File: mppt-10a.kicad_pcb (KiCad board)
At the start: 2 copper layers, 80 x 80 mm, 133 parts, among them J1 SOLAR, J2 LOAD, J3 BAT, J4 UEXT, J5 USB_A_stacked, P1 CONN_01X02, Q1 PSMN5R2-60YLX, Q2 PSMN5R2-60YLX, Q3 PSMN5R2-60YLX, Q4 PSMN5R2-60YLX, SW2 SW_PUSH, T1 MMBT3904, T3 MMBT3904, U1 LM5109BMA, U2 STM32F072CB, U3 AP22802A, U4 IP4220CZ6, U5 AP2210-3.3, U6 24AA01, U7 LM258, U8 TPS2513, U9 AP6502, Y1 8MHz

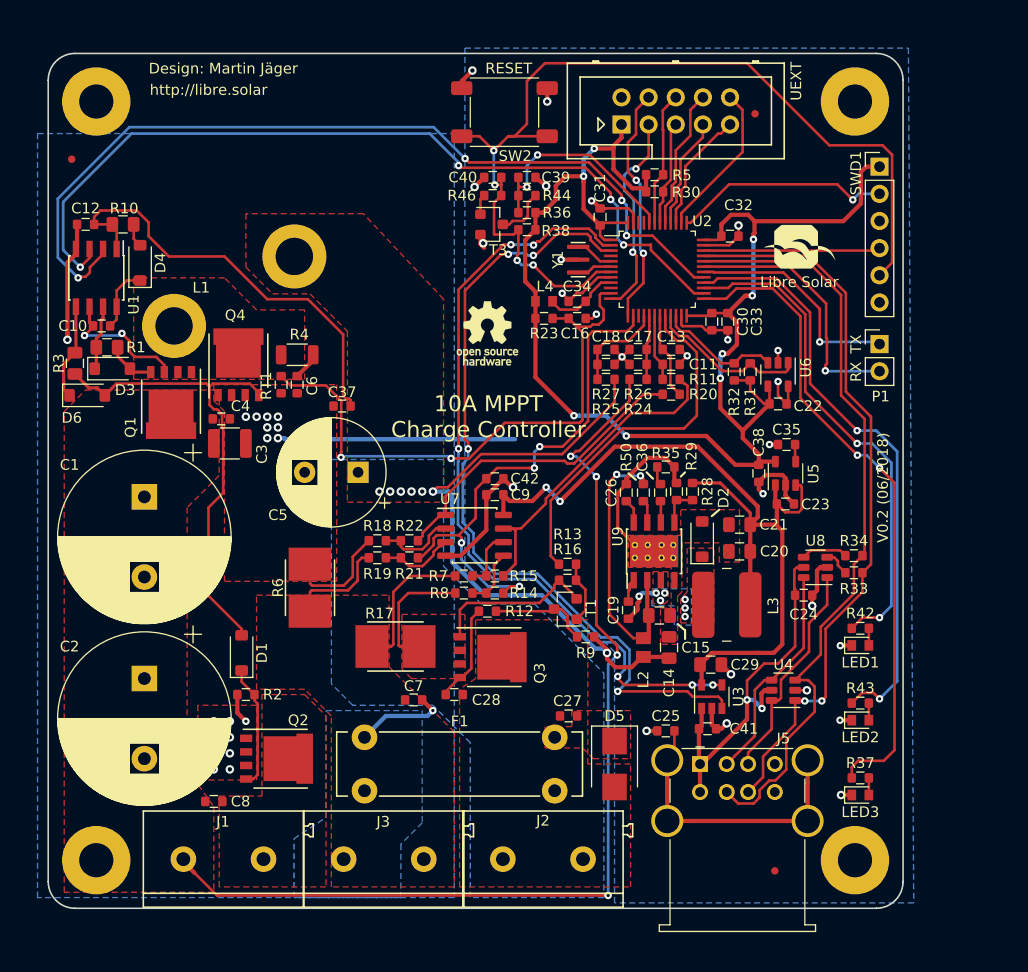
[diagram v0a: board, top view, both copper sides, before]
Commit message: Several improvements (v0.4) after first tests
- Ultra-low-power MCU STM32L072
- Larger screw terminals
- USB power supply replaced by more efficient SMPS
- High-side load switch with P-MOS
- High-side current measurement to include USB current in load measurement
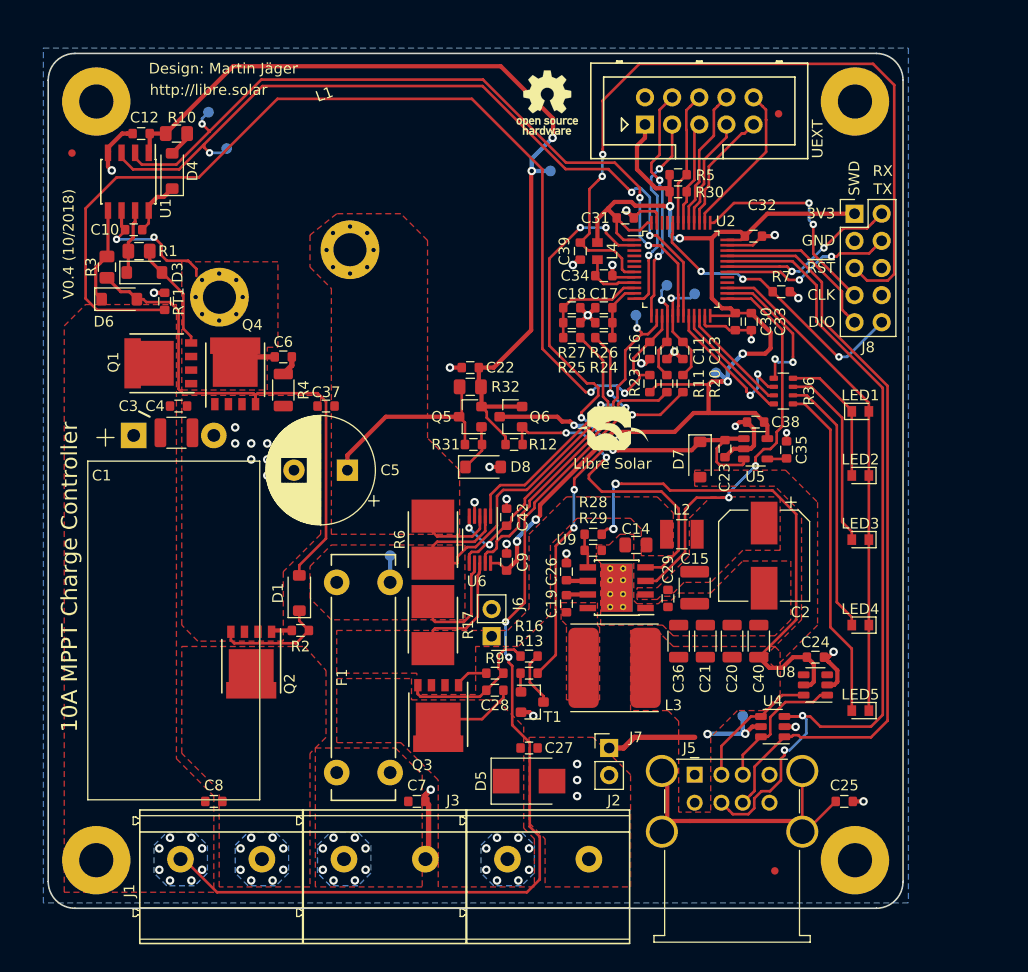
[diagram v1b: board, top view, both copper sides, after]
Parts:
- removed C41: 100n, LibreSolar:C_0603_1608
- removed D2: SS14FL, LibreSolar:D_SOD-123
- removed P1: CONN_01X02, Connector_PinHeader_2.54mm:PinHeader_1x02_P2.54mm_Vertical
- removed R14, R15, R21, R22: 150k, LibreSolar:R_0603_1608
- removed R18, R19, R44, R8: 2.2k, LibreSolar:R_0603_1608
- removed R33, R34: 0R, LibreSolar:R_0603_1608
- removed R35: 6.8k, LibreSolar:R_0603_1608
- removed R37, R42, R43: 470, LibreSolar:R_0603_1608
- removed R38: 1M, LibreSolar:R_0603_1608
- removed R46: 56k, LibreSolar:R_0603_1608
- removed R50: 100k, LibreSolar:R_0603_1608
- removed SW2: SW_PUSH, LibreSolar:SW_SPST_6mm
- removed SWD1: ST_Nucleo_SWD, Connector_PinHeader_2.54mm:PinHeader_1x06_P2.54mm_Vertical
- removed T3: MMBT3904, LibreSolar:SOT-23
- removed U3: AP22802A, Package_TO_SOT_SMD:SOT-23-5
- removed U7: LM258, LibreSolar:SOIC-8_3.9x4.9mm_Pitch1.27mm
- removed Y1: 8MHz, LibreSolar:Resonator_Murata_CSTCE_G
- added D7: 1N4148, LibreSolar:D_SOD-123, F.Cu at (159.5, 96.0)
- added D8: 11V, LibreSolar:D_SOD-123, F.Cu at (139.2, 96.7)
- added J6: PWR_12V, Connector_PinHeader_2.54mm:PinHeader_1x02_P2.54mm_Vertical, F.Cu at (140.0, 112.5)
- added J7: PWR_5V, Connector_PinHeader_2.54mm:PinHeader_1x02_P2.54mm_Vertical, F.Cu at (151.0, 123.0)
- added J8: Conn_02x05_Odd_Even, Connector_PinHeader_2.54mm:PinHeader_2x05_P2.54mm_Vertical, F.Cu at (174.0, 73.0)
- added LED4: green, LED_SMD:LED_0603_1608Metric, F.Cu at (174.5, 111.5)
- added LED5: green, LED_SMD:LED_0603_1608Metric, F.Cu at (174.5, 119.5)
- added Q5: BSS138N, LibreSolar:SOT-23, F.Cu at (138.0, 92.0)
- added Q6: DMP3099L-7, LibreSolar:SOT-23, F.Cu at (141.8, 92.0)
- added TP1: Test_Point_Probe, TestPoint:TestPoint_Pad_D1.0mm, B.Cu at (130.5, 105.0)
- added TP2: Test_Point_Probe, TestPoint:TestPoint_Pad_D1.0mm, B.Cu at (113.5, 63.5)
- added TP3: Test_Point_Probe, TestPoint:TestPoint_Pad_D1.0mm, B.Cu at (115.2, 66.9)
- added TP4: Test_Point_Probe, TestPoint:TestPoint_Pad_D1.0mm, B.Cu at (159.0, 80.5)
- added TP5: Test_Point_Probe, TestPoint:TestPoint_Pad_D1.0mm, B.Cu at (156.4, 79.7)
- added TP6: Test_Point_Probe, TestPoint:TestPoint_Pad_D1.0mm, B.Cu at (153.5, 82.5)
- added TP7: Test_Point_Probe, TestPoint:TestPoint_Pad_D1.0mm, B.Cu at (163.5, 120.0)
- added TP8: Test_Point_Probe, TestPoint:TestPoint_Pad_D1.0mm, B.Cu at (145.5, 69.0)
- added TP9: Test_Point_Probe, TestPoint:TestPoint_Pad_D1.0mm, B.Cu at (161.0, 87.9)
- C1: value 680u -> 1200u; footprint Capacitor_THT:CP_Radial_D16.0mm_P7.50mm -> LibreSolar:CP_Radial_L31.5mm_D16.0mm_P7.50mm_horizontal
- C15: value 22u -> 10u; footprint LibreSolar:C_0805_2012 -> LibreSolar:C_1210_3225
- C2: value 680u -> 150u; footprint Capacitor_THT:CP_Radial_D16.0mm_P7.50mm -> Capacitor_SMD:CP_Elec_8x6.2
- C20, C21: value 47u -> 22u; footprint LibreSolar:C_0805_2012 -> LibreSolar:C_1206_3216
- C22: value 100n -> 2.2u
- C29: value 1u -> 220n; footprint LibreSolar:C_0805_2012 -> LibreSolar:C_0603_1608
- C36: value 6.8n -> 22u; footprint LibreSolar:C_0603_1608 -> LibreSolar:C_1206_3216
- C39: value 2.2u -> 100n
- C40: value 100n -> 22u; footprint LibreSolar:C_0603_1608 -> LibreSolar:C_1206_3216
- J1, J2, J3: footprint LibreSolar:Phoenix_Contact_PT_2,5-2-7,5-H -> LibreSolar:Phoenix_Contact_MKDS_5-2-7,62
- L1: footprint LibreSolar:L-FERYSTER-DTMSS-27 -> LibreSolar:L-FERYSTER-DTMSS-27_33uH
- L2: footprint Inductor_SMD:L_0805_2012Metric -> Inductor_SMD:L_1210_3225Metric
- L3: footprint LibreSolar:Bourns_SRN6045TA -> LibreSolar:Bourns_SRN8040TA
- LED1: value LED_red -> red
- LED2, LED3: value LED_green -> red
- Q3: value PSMN5R2-60YLX -> BSC084P03NS3
- R12: value 2.2k -> 100k
- R27: value 10k -> 5.6k
- R28: value 45.3k -> 100k
- R29: value 10k -> 24.9k
- R31: value 2.2k -> 10k
- R32: value 2.2k -> 4.7; footprint LibreSolar:R_0603_1608 -> LibreSolar:R_0805_2012
- R36: value 1M -> 680; footprint LibreSolar:R_0603_1608 -> LibreSolar:R_Array_Convex_4x0603
- R9: value 56k -> 10k
- U2: value STM32F072CB -> STM32L072CZT6
- U6: value 24AA01 -> INA2181; footprint LibreSolar:SOT-23-5 -> LibreSolar:VSSOP-10_3.0x3.0mm_P0.5mm
- U9: value AP6502 -> LMR33630
- moved C2 59.1 mm to (165.5, 105.0)
- moved C40 50.0 mm to (165.0, 113.0), turned to 90 degrees
- moved R7 39.9 mm to (167.1, 80.3), turned to 0 degrees
- moved U6 31.9 mm to (138.9, 103.5)
- moved R36 29.2 mm to (167.3, 89.6)
- moved C22 29.0 mm to (138.0, 87.4), turned to 180 degrees
- moved R31 26.8 mm to (138.3, 94.6), turned to 180 degrees
- moved R32 24.7 mm to (138.0, 89.2), turned to 0 degrees
- moved LOGO1 24.4 mm to (149.0, 95.1)
- moved LED3 23.9 mm to (174.5, 103.5), turned to 180 degrees
- moved LED2 22.9 mm to (174.5, 97.5), turned to 180 degrees
- moved LOGO2 22.3 mm to (145.2, 62.6)
- moved LED1 21.9 mm to (174.5, 91.5)
- moved C25 18.0 mm to (173.0, 128.0), turned to 0 degrees
- moved R12 15.8 mm to (142.1, 94.6), turned to 180 degrees
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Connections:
- net /MCU/USB_DM renamed USB_DM
- net /MCU/USB_DP renamed USB_DP
- net Net-(U2-Pad45) renamed /MCU/CAN_RX
- net Net-(U2-Pad46) renamed /MCU/CAN_TX
- C1 pad 1: /DCDC power stage/DCDC_IN -> DCDC_IN
- C11 pad 1: /MCU/I_LOAD -> I_LOAD
- C12 pad 1: +12V -> +10V
- C13 pad 1: /MCU/I_DCDC -> I_DCDC
- C14 pad 1: +12V -> LOAD_S
- C16 pad 1: /Analog Frontend/TEMP_INT -> T_MOSFETS
- C17 pad 1: /MCU/V_SOLAR -> V_SOLAR
- C18 pad 1: /MCU/V_BAT -> V_BAT
- C2 pad 1: /DCDC power stage/DCDC_IN -> Net-(C15-Pad1)
- C22 pad 1: +3V3 -> +10V
- C23 pad 1: +5V -> Net-(C23-Pad1)
- C24 pad 1: Net-(C24-Pad1) -> +5V
- C27 pad 1: +12V -> LOAD+
- C27 pad 2: /DCDC power stage/LOAD- -> GND
- C28 pad 1: Net-(C28-Pad1) -> LOAD+
- C28 pad 2: /DCDC power stage/LOAD- -> Net-(C28-Pad2)
- C29 pad 1: +5V -> Net-(C15-Pad1)
- C3 pad 1: /DCDC power stage/DCDC_IN -> DCDC_IN
- C36 pad 1: Net-(C36-Pad1) -> +5V
- C36 pad 2: Net-(C36-Pad2) -> GND
- C37 pad 1: +12V -> DCDC_OUT
- C39 pad 1: /MCU/BOOT0 -> /MCU/~RESET
- C4 pad 1: /DCDC power stage/DCDC_IN -> DCDC_IN
- C40 pad 1: /MCU/~RESET -> +5V
- C42 pad 1: /MCU/DAC -> DAC
- C5 pad 1: +12V -> DCDC_OUT
- C6 pad 1: Net-(C6-Pad1) -> /DCDC power stage/SW_NODE
- C6 pad 2: GND -> Net-(C6-Pad2)
- C7 pad 2: /DCDC power stage/BAT- -> GND
- C8 pad 1: /DCDC power stage/DCDC_IN -> DCDC_IN
- C9 pad 1: +5V -> +3V3
- D5 pad 1: +12V -> LOAD+
- D5 pad 2: /DCDC power stage/LOAD- -> GND
- J1 pad 1: /DCDC power stage/DCDC_IN -> DCDC_IN
- J2 pad 1: /DCDC power stage/LOAD- -> LOAD+
- J2 pad 2: +12V -> GND
- J3 pad 2: /DCDC power stage/BAT- -> GND
- J5 pad 1: Net-(C24-Pad1) -> +5V
- J5 pad 5: Net-(C24-Pad1) -> +5V
- L1 pad 2: +12V -> DCDC_OUT
- L2 pad 1: +12V -> LOAD_S
- LED1 pad 1: GND -> Net-(LED1-Pad1)
- LED1 pad 2: Net-(LED1-Pad2) -> /MCU/LED_GND
- LED2 pad 1: GND -> /MCU/LED_GND
- LED2 pad 2: Net-(LED2-Pad2) -> Net-(LED1-Pad1)
- LED3 pad 1: GND -> /MCU/LED_GND
- Q1 pad D: /DCDC power stage/DCDC_IN -> DCDC_IN
- Q3 pad D: /DCDC power stage/LOAD- -> LOAD+
- Q3 pad G: Net-(C28-Pad1) -> Net-(C28-Pad2)
- Q3 pad S: /DCDC power stage/LOAD-SW -> LOAD_S
- R10 pad 2: +12V -> +10V
- R11 pad 2: /MCU/I_LOAD -> I_LOAD
- R12 pad 1: Net-(C28-Pad1) -> /Power Supply/PG_5V
- R12 pad 2: Net-(R12-Pad2) -> +10V
- R13 pad 2: /DCDC power stage/~LOAD_EN -> LOAD_EN
- R16 pad 1: /DCDC power stage/LOAD-SW -> Net-(R16-Pad1)
- R16 pad 2: Net-(R13-Pad1) -> Net-(C28-Pad2)
- R17 pad 1: /DCDC power stage/BAT- -> +12V
- R17 pad 2: /DCDC power stage/LOAD-SW -> LOAD_S
- R20 pad 2: /MCU/I_DCDC -> I_DCDC
- R23 pad 2: /Analog Frontend/TEMP_INT -> T_MOSFETS
- R24 pad 1: /DCDC power stage/DCDC_IN -> DCDC_IN
- R24 pad 2: /MCU/V_SOLAR -> V_SOLAR
- R25 pad 2: /MCU/V_BAT -> V_BAT
- R26 pad 1: /MCU/V_SOLAR -> V_SOLAR
- R27 pad 1: /MCU/V_BAT -> V_BAT
- R31 pad 1: /MCU/I2C2_SCL -> Net-(D8-Pad1)
- R31 pad 2: +3V3 -> DCDC_OUT
- R32 pad 1: /MCU/I2C2_SDA -> DCDC_OUT
- R32 pad 2: +3V3 -> +10V
- R36 pad 1: /MCU/BOOT0 -> /MCU/LED_SOC_12
- R36 pad 2: +3V3 -> Net-(LED1-Pad1)
- R4 pad 1: Net-(C6-Pad1) -> GND
- R4 pad 2: /DCDC power stage/SW_NODE -> Net-(C6-Pad2)
- R6 pad 1: GND -> DCDC_OUT
- R6 pad 2: /DCDC power stage/BAT- -> +12V
- R7 pad 1: Net-(R15-Pad1) -> /MCU/BOOT0
- R7 pad 2: /DCDC power stage/BAT- -> GND
- R9 pad 1: Net-(R12-Pad2) -> Net-(C28-Pad2)
- R9 pad 2: +12V -> LOAD_S
- RT1 pad 1: /Analog Frontend/TEMP_INT -> T_MOSFETS
- T1 pad 2: /DCDC power stage/LOAD-SW -> GND
- T1 pad 3: Net-(R12-Pad2) -> Net-(R16-Pad1)
- U1 pad 1: +12V -> +10V
- U1 pad 2: /DCDC power stage/PWM_HS -> PWM_HS
- U1 pad 3: /DCDC power stage/PWM_LS -> PWM_LS
- U2 pad 10: /MCU/TEMP_BAT -> V_BAT
- U2 pad 11: /Analog Frontend/TEMP_INT -> V_SOLAR
- U2 pad 14: /MCU/DAC -> DAC
- U2 pad 15: /MCU/V_REF -> T_MOSFETS
- U2 pad 16: /MCU/V_BAT -> I_LOAD
- U2 pad 17: /MCU/V_SOLAR -> I_DCDC
- U2 pad 18: /MCU/I_LOAD -> PWM_HS
- U2 pad 19: /MCU/I_DCDC -> PWM_LS
- U2 pad 2: /MCU/USB_PWR_EN -> LOAD_EN
- U2 pad 20: /DCDC power stage/~LOAD_EN -> /MCU/LED_SOC_3
- U2 pad 21: /MCU/I2C2_SCL -> /MCU/LED_LOAD
- U2 pad 22: /MCU/I2C2_SDA -> /MCU/LED_SOLAR
- U2 pad 25: /MCU/LED3 -> USB_PWR_EN
- U2 pad 26: /DCDC power stage/PWM_LS -> /MCU/LED_SOC_12
- U2 pad 27: /MCU/LED1 -> /MCU/LED_GND
- U2 pad 28: /MCU/LED2 -> Net-(U2-Pad28)
- U2 pad 29: /DCDC power stage/PWM_HS -> Net-(U2-Pad29)
- U2 pad 3: /MCU/USB_PWR_FLG -> Net-(U2-Pad3)
- U4 pad 5: Net-(C24-Pad1) -> +5V
- U5 pad 1: +5V -> Net-(C23-Pad1)
- U5 pad 3: +5V -> Net-(C23-Pad1)
- U6 pad 1: /MCU/I2C2_SCL -> Net-(R20-Pad1)
- U6 pad 2: GND -> +12V
- U6 pad 3: /MCU/I2C2_SDA -> DCDC_OUT
- U6 pad 4: +3V3 -> GND
- U6 pad 5: GND -> DAC
- U8 pad 5: Net-(C24-Pad1) -> +5V
- U9 pad 1: Net-(C19-Pad1) -> GND
- U9 pad 3: Net-(C19-Pad2) -> USB_PWR_EN
- U9 pad 4: GND -> /Power Supply/PG_5V
- U9 pad 6: Net-(C36-Pad1) -> Net-(C26-Pad1)
- U9 pad 7: Net-(R50-Pad1) -> Net-(C19-Pad1)
- U9 pad 8: Net-(C26-Pad1) -> Net-(C19-Pad2)
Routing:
- net T_MOSFETS: track 0.00 -> 102.9 mm, vias 0 -> 2
- net /DCDC power stage/DCDC_IN: track 94.5 -> 0.00 mm, vias 4 -> 0
- net DCDC_IN: track 0.00 -> 93.0 mm, vias 0 -> 12
- net +10V: track 0.00 -> 84.8 mm, vias 0 -> 2
- net /DCDC power stage/PWM_HS: track 83.2 -> 0.00 mm, vias 4 -> 0
- net /DCDC power stage/PWM_LS: track 80.3 -> 0.00 mm, vias 4 -> 0
- net /MCU/USB_PWR_FLG: track 75.7 -> 0.00 mm, vias 4 -> 0
- net PWM_LS: track 0.00 -> 73.8 mm, vias 0 -> 3
- net /MCU/USB_PWR_EN: track 73.8 -> 0.00 mm, vias 6 -> 0
- net GND: track 138.2 -> 65.0 mm, vias 44 -> 34
- net PWM_HS: track 0.00 -> 71.9 mm, vias 0 -> 3
- net /MCU/LED3: track 60.9 -> 0.00 mm, vias 2 -> 0
- net LOAD_EN: track 0.00 -> 57.4 mm, vias 0 -> 6
- net /MCU/LED2: track 55.9 -> 0.00 mm, vias 2 -> 0
- net /Analog Frontend/TEMP_INT: track 54.0 -> 0.00 mm, vias 2 -> 0
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- added copper zone on F.Cu, net +5V
- added copper zone on F.Cu, net /DCDC power stage/BAT+
- added copper zone on B.Cu, net /DCDC power stage/SOLAR-
- added copper zone on B.Cu, net DCDC_IN
- added copper zone on F.Cu, net DCDC_IN
- added copper zone on F.Cu, net DCDC_OUT
- added copper zone on B.Cu, net LOAD+
- added copper zone on F.Cu, net LOAD+
- added copper zone on F.Cu, net LOAD_S
- added copper zone on F.Cu, net Net-(C15-Pad1)
- removed copper zone on B.Cu, net +12V
- removed copper zone on F.Cu, net /DCDC power stage/BAT-
- removed copper zone on F.Cu, net /DCDC power stage/DCDC_IN
- removed copper zone on F.Cu, net /DCDC power stage/LOAD-
- removed copper zone on F.Cu, net /DCDC power stage/LOAD-SW
- removed copper zone on B.Cu, net Net-(C19-Pad2)
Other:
- board text added: "CLK"
- board text added: "DIO"
- board text added: "SWD"
- board text added: "V0.4 (10/2018)"
- board text added: "~RST"
- board text removed: "RESET"
- board text removed: "SW"
- board text removed: "V0.2 (06/2018)"

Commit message: Board shape adjusted and 6P6C connector added
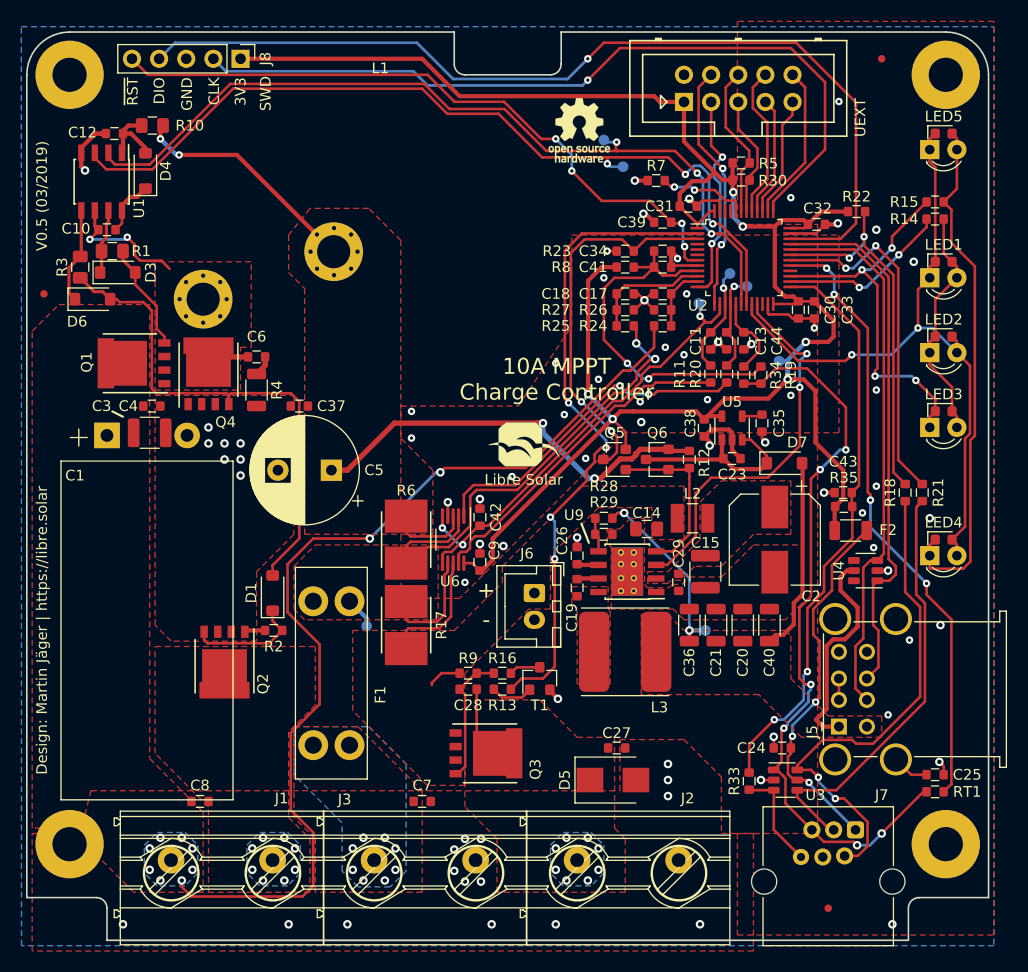
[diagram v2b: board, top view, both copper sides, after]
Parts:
- removed C16: 100n, LibreSolar:C_0603_1608
- removed C22: 2.2u, LibreSolar:C_0603_1608
- removed D8: 11V, LibreSolar:D_SOD-123
- removed L4: 600R, Inductor_SMD:L_0603_1608Metric
- removed R31: 10k, LibreSolar:R_0603_1608
- removed R32: 4.7, LibreSolar:R_0805_2012
- removed R36: 680, LibreSolar:R_Array_Convex_4x0603
- removed TP8: Test_Point_Probe, TestPoint:TestPoint_Pad_D1.0mm
- removed U8: TPS2513, LibreSolar:SOT-23-6
- added C41: 10n, LibreSolar:C_0603_1608, F.Cu at (156.0, 78.0)
- added C43: 100n, LibreSolar:C_0603_1608, F.Cu at (172.9, 99.1)
- added C44: 10n, LibreSolar:C_0603_1608, F.Cu at (163.6, 84.9)
- added F2: 50mA, LibreSolar:R_1206_3216, F.Cu at (173.6, 102.7)
- added R14: 470, LibreSolar:R_0603_1608, F.Cu at (181.5, 73.5)
- added R15: 470, LibreSolar:R_0603_1608, F.Cu at (181.5, 71.9)
- added R18: 470, LibreSolar:R_0603_1608, F.Cu at (178.7, 99.1)
- added R19: 10k, LibreSolar:R_0603_1608, F.Cu at (165.2, 88.1)
- added R21: 470, LibreSolar:R_0603_1608, F.Cu at (180.3, 99.1)
- added R22: 100k, LibreSolar:R_0603_1608, F.Cu at (174.2, 72.8)
- added R33: 2.2k, LibreSolar:R_0603_1608, F.Cu at (164.1, 126.1)
- added R34: 2.2k, LibreSolar:R_0603_1608, F.Cu at (163.6, 88.1)
- added R35: 100k, LibreSolar:R_0603_1608, F.Cu at (172.9, 100.4)
- added R8: 100, LibreSolar:R_0603_1608, F.Cu at (152.5, 78.0)
- added U3: D1213A-04SO, LibreSolar:SOT-23-6, F.Cu at (167.5, 126.0)
- C34: value 100n -> 2.2u
- F1: footprint LibreSolar:Fuse_Clip_5x20mm -> LibreSolar:KEYSTONE-FUSE-3557-2
- J1: value SOLAR -> MKDS_5-2_952; footprint LibreSolar:Phoenix_Contact_MKDS_5-2-7,62 -> LibreSolar:Phoenix_Contact_MKDS_5-2-952
- J2: value LOAD -> MKDS_5-2_952; footprint LibreSolar:Phoenix_Contact_MKDS_5-2-7,62 -> LibreSolar:Phoenix_Contact_MKDS_5-2-952
- J3: value BAT -> MKDS_5-2_952; footprint LibreSolar:Phoenix_Contact_MKDS_5-2-7,62 -> LibreSolar:Phoenix_Contact_MKDS_5-2-952
- J6: footprint Connector_PinHeader_2.54mm:PinHeader_1x02_P2.54mm_Vertical -> Connector_JST:JST_XH_B02B-XH-A_1x02_P2.50mm_Vertical
- J7: value PWR_5V -> 6P6C; footprint Connector_PinHeader_2.54mm:PinHeader_1x02_P2.54mm_Vertical -> LibreSolar:RJ25_6P6C_TabUp
- J8: value Conn_02x05_Odd_Even -> ST_Nucleo_SWD; footprint Connector_PinHeader_2.54mm:PinHeader_2x05_P2.54mm_Vertical -> Connector_PinHeader_2.54mm:PinHeader_1x05_P2.54mm_Vertical
- LED1, LED2, LED3: value red -> yellow; footprint LED_SMD:LED_0603_1608Metric -> LibreSolar:LED_0603_D3.0mm
- LED4, LED5: footprint LED_SMD:LED_0603_1608Metric -> LibreSolar:LED_0603_D3.0mm
- Q5: value BSS138N -> DMP3099L-7
- R17, R6: value 4m -> 3m
- R23: value 10k -> 100k
- RT1: value 10k -> 10k NTC
- U4: value IP4220CZ6 -> D1213A-04SO
- moved RT1 85.5 mm to (181.5, 127.1), turned to 0 degrees
- moved J8 59.3 mm to (116.5, 58.5), turned to 270 degrees
- moved LED5 54.6 mm to (182.3, 65.5), turned to 0 degrees
- moved TP3 37.1 mm to (152.3, 68.6)
- moved TP2 37.1 mm to (150.5, 66.1)
- moved J7 24.0 mm to (171.5, 135.5)
- moved U4 17.0 mm to (175.0, 106.4)
- moved R12 16.5 mm to (158.5, 96.0), turned to 90 degrees
- moved LED1 16.0 mm to (182.3, 77.5)
- moved R7 15.7 mm to (155.4, 69.9), turned to 180 degrees
- moved LED2 15.2 mm to (182.3, 84.5), turned to 0 degrees
- moved LED3 14.3 mm to (182.3, 91.5), turned to 0 degrees
- moved Q6 14.3 mm to (155.5, 96.0)
- moved J5 14.2 mm to (172.5, 121.0), turned to 90 degrees
- moved Q5 14.1 mm to (151.5, 96.0)
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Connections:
- net /MCU/CAN_RX renamed Net-(U2-Pad45)
- net /MCU/CAN_TX renamed Net-(U2-Pad46)
- net /MCU/OSC_IN renamed Net-(U2-Pad5)
- net /MCU/OSC_OUT renamed Net-(U2-Pad6)
- net DCDC_IN renamed /DCDC power stage/SOLAR+
- net Net-(C34-Pad1) renamed VDDA
- C12 pad 1: +10V -> Net-(C12-Pad1)
- C24 pad 1: +5V -> Net-(C24-Pad1)
- D4 pad 2: Net-(D4-Pad2) -> Net-(C12-Pad1)
- J5 pad 3: Net-(J5-Pad3) -> Net-(J5-Pad2)
- J7 pad 1: +5V -> Net-(C24-Pad1)
- J7 pad 2: GND -> Net-(J7-Pad2)
- J8 pad 2: /MCU/USART1_RX -> /MCU/SWCLK
- J8 pad 4: /MCU/USART1_TX -> /MCU/SWDIO
- LED1 pad 1: Net-(LED1-Pad1) -> /MCU/LED_C
- LED1 pad 2: /MCU/LED_GND -> Net-(LED1-Pad2)
- LED2 pad 1: /MCU/LED_GND -> Net-(LED1-Pad2)
- LED2 pad 2: Net-(LED1-Pad1) -> /MCU/LED_C
- LED3 pad 1: /MCU/LED_GND -> /MCU/LED_B
- LED3 pad 2: Net-(LED3-Pad2) -> Net-(LED1-Pad2)
- LED4 pad 1: /MCU/LED_GND -> Net-(LED4-Pad1)
- LED4 pad 2: Net-(LED4-Pad2) -> /MCU/LED_C
- LED5 pad 1: /MCU/LED_GND -> /MCU/LED_C
- LED5 pad 2: Net-(LED5-Pad2) -> Net-(LED4-Pad1)
- MK4 pad 1: Net-(MK4-Pad1) -> GND
- Q5 pad 1: Net-(D8-Pad1) -> Net-(Q5-Pad1)
- Q5 pad 2: +10V -> +3V3
- Q5 pad 3: DCDC_OUT -> 5V_PG
- Q6 pad 1: /Power Supply/PG_5V -> Net-(Q5-Pad1)
- Q6 pad 2: +10V -> DCDC_OUT
- R10 pad 1: Net-(D4-Pad2) -> Net-(C12-Pad1)
- R10 pad 2: +10V -> DCDC_OUT
- R12 pad 1: /Power Supply/PG_5V -> Net-(Q5-Pad1)
- R12 pad 2: +10V -> DCDC_OUT
- R23 pad 1: +3V3 -> GND
- R23 pad 2: T_MOSFETS -> 5V_PG
- RT1 pad 1: T_MOSFETS -> /MCU/TEMP_EXT
- RT1 pad 2: GND -> /MCU/TEMP_INT_PD
- U1 pad 1: +10V -> Net-(C12-Pad1)
- U2 pad 15: T_MOSFETS -> I_LOAD
- U2 pad 16: I_LOAD -> I_DCDC
- U2 pad 17: I_DCDC -> T_BAT
- U2 pad 20: /MCU/LED_SOC_3 -> /MCU/LED_C
- U2 pad 21: /MCU/LED_LOAD -> USB_PWR_EN
- U2 pad 22: /MCU/LED_SOLAR -> Net-(U2-Pad22)
- U2 pad 25: USB_PWR_EN -> /MCU/BUTTON
- U2 pad 26: /MCU/LED_SOC_12 -> /MCU/LED_A
- U2 pad 27: /MCU/LED_GND -> /MCU/LED_B
- U2 pad 29: Net-(U2-Pad29) -> /MCU/TEMP_INT_PD
- U2 pad 3: Net-(U2-Pad3) -> 5V_PG
- U4 pad 4: Net-(J5-Pad2) -> Net-(U4-Pad4)
- U4 pad 6: Net-(J5-Pad3) -> Net-(U4-Pad6)
- U9 pad 4: /Power Supply/PG_5V -> Net-(Q5-Pad1)
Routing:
- net T_MOSFETS: track 102.9 -> 0.00 mm, vias 2 -> 0
- net +10V: track 84.8 -> 0.00 mm, vias 2 -> 0
- net /MCU/SWDIO: track 15.7 -> 89.0 mm, vias 0 -> 1
- net /MCU/TEMP_EXT: track 0.00 -> 70.6 mm, vias 0 -> 6
- net +3V3: track 122.9 -> 188.9 mm
- net /MCU/LED_C: track 0.00 -> 65.6 mm, vias 0 -> 2
- net /MCU/TEMP_INT_PD: track 0.00 -> 57.6 mm, vias 0 -> 4
- net /MCU/SWCLK: track 20.4 -> 75.1 mm, vias 2 -> 1
- net /MCU/BUTTON: track 0.00 -> 54.3 mm, vias 0 -> 2
- net Net-(LED4-Pad1): track 0.00 -> 49.1 mm
- net Net-(J7-Pad2): track 0.00 -> 47.4 mm, vias 0 -> 2
- net /MCU/LED_GND: track 46.5 -> 0.00 mm
- net DCDC_OUT: track 26.3 -> 68.7 mm, vias 8 -> 12
- net Net-(J7-Pad3): track 0.00 -> 40.0 mm
- net /MCU/LED_B: track 0.00 -> 36.3 mm, vias 0 -> 4
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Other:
- board size 80 x 80 mm -> 90 x 85 mm
- board text added: "Design: Martin Jäger | https://libre.solar"
- board text added: "V0.5 (03/2019)"
- board text removed: "Design: Martin Jäger"
- board text removed: "V0.4 (10/2018)"
- board text removed: "http://libre.solar"

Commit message: Solar voltage input protection added
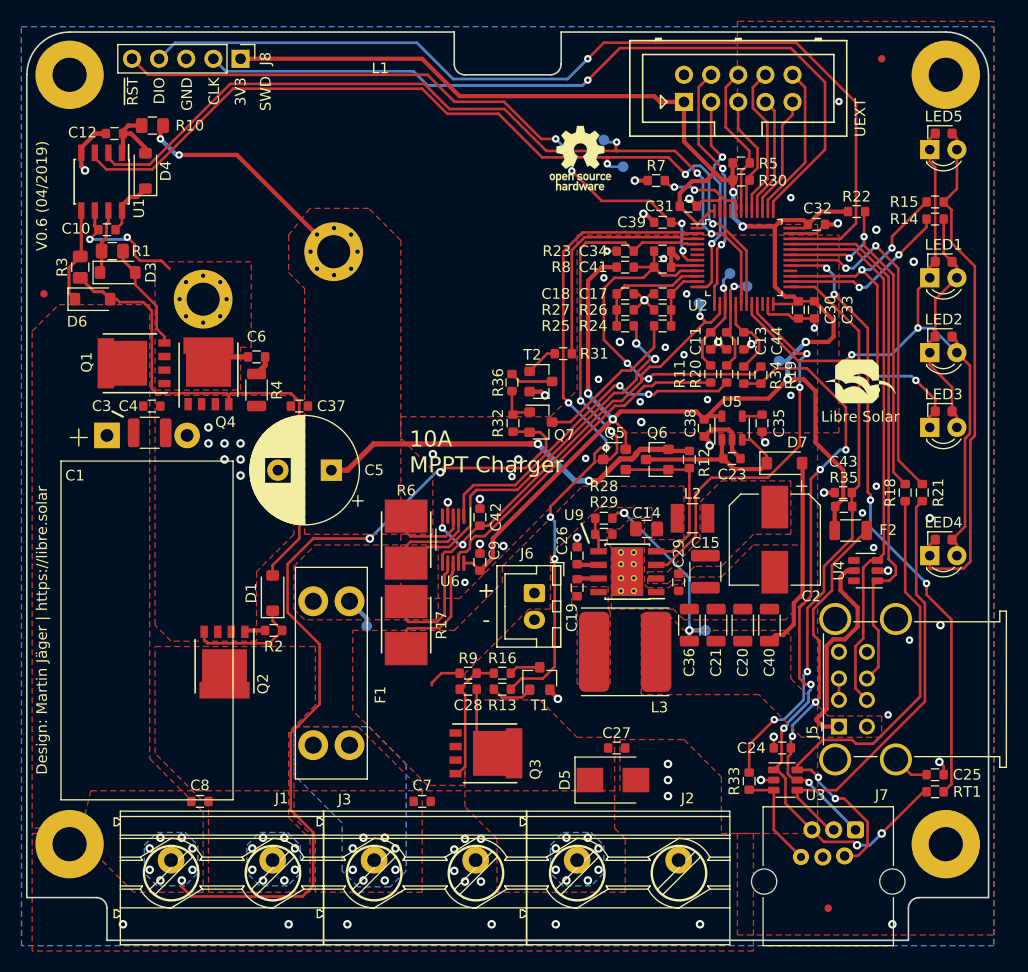
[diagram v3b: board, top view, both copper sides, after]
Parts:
- added Q7: BSS83P, LibreSolar:SOT-23, F.Cu at (144.6, 92.5)
- added R31: 10k, LibreSolar:R_0603_1608, F.Cu at (146.7, 86.1)
- added R32: 1M, LibreSolar:R_0603_1608, F.Cu at (142.0, 92.6)
- added R36: 10k, LibreSolar:R_0603_1608, F.Cu at (141.9, 88.8)
- added T2: MMBT3904, LibreSolar:SOT-23, F.Cu at (144.6, 88.7)
- Q5, Q6: value DMP3099L-7 -> BSS83P
- moved LOGO1 32.0 mm to (172.2, 90.7)
- moved LOGO2 2.60 mm to (148.3, 67.8)
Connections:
- R24 pad 1: /DCDC power stage/SOLAR+ -> Net-(Q7-Pad3)
- U2 pad 3: 5V_PG -> V_SOLAR_EN
- U2 pad 4: Net-(U2-Pad4) -> 5V_PG
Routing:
- net V_SOLAR_EN: track 0.00 -> 22.0 mm
- net Net-(Q7-Pad3): track 0.00 -> 14.4 mm
- net /DCDC power stage/SOLAR+: track 91.7 -> 80.1 mm
- net Net-(R36-Pad1): track 0.00 -> 4.04 mm
- net Net-(Q7-Pad1): track 0.00 -> 3.89 mm
- net Net-(R31-Pad1): track 0.00 -> 3.10 mm
- net DCDC_OUT: track 68.7 -> 66.8 mm
- net GND: track 57.8 -> 59.4 mm, vias 76 -> 75
- net 5V_PG: track 35.3 -> 34.0 mm
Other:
- board text added: "10A MPPT Charger"
- board text added: "V0.6 (04/2019)"
- board text removed: "10A MPPT Charge Controller"
- board text removed: "V0.5 (03/2019)"
